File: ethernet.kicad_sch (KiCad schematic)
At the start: 27 parts, among them U5 W5500, Y1 25MHz

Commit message: Stuff.
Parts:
- C15: LCSC (none) -> C466237
- C17: LCSC (none) -> C2911388
- C4, C8: value 18p -> 22p; LCSC C555395 -> (none)
- U5: LCSC (none) -> C32843
- Y1: LCSC (none) -> C5563795
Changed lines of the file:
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@@
 			)
 		)
-		(property "Datasheet" ""
+		(property "Datasheet" "https://jlcpcb.com/partdetail/Sanyear-C0402X5R475M250NT/C2911388"
 			(at 129.54 119.38 0)
 			(effects
@@
 			)
 		)
+		(property "LCSC" "C2911388"
+			(at 129.54 119.38 0)
+			(effects
+				(font
+					(size 1.27 1.27)
+				)
+				(hide yes)
+			)
+		)
 		(pin "2"
 		)
@@
 			)
 		)
-		(property "Value" "18p"
+		(property "Value" "22p"
 			(at 210.566 100.076 0)
 			(effects
@@
 			)
 		)
-		(property "Description" "Unpolarized capacitor"
+		(property "Description" ""
 			(at 210.82 97.79 0)
 			(effects
@@
 			)
 		)
-		(property "LCSC" "C555395"
+		(property "LCSC" ""
 			(at 210.82 97.79 0)
 			(effects
@@
 			)
 		)
-		(property "Datasheet" ""
+		(property "Datasheet" "https://www.lcsc.com/product-detail/Crystal-Oscillators_HCI-1532H4-25000J18DTSTL_C5563795.html"
 			(at 205.74 90.17 0)
 			(effects
@@
 			)
 		)
-		(property "LCSC" ""
+		(property "LCSC" "C5563795"
 			(at 205.74 90.17 0)
 			(effects
@@
 			)
 		)
-		(property "Datasheet" ""
+		(property "Datasheet" "https://jlcpcb.com/partdetail/Cctc-TCC0402X7R223K250AT/C466237"
 			(at 143.51 90.17 0)
 			(effects
@@
 			)
 		)
+		(property "LCSC" "C466237"
+			(at 143.51 90.17 0)
+			(effects
+				(font
+					(size 1.27 1.27)
+				)
+				(hide yes)
+			)
+		)
 		(pin "2"
 		)
@@
 			)
 		)
+		(property "LCSC" "C32843"
+			(at 172.72 86.36 0)
+			(effects
+				(font
+					(size 1.27 1.27)
+				)
+				(hide yes)
+			)
+		)
 		(pin "38"
 		)
@@
 			)
 		)
-		(property "Value" "18p"
+		(property "Value" "22p"
 			(at 200.406 100.076 0)
 			(effects
@@
 			)
 		)
-		(property "Description" "Unpolarized capacitor"
+		(property "Description" ""
 			(at 200.66 97.79 0)
 			(effects
@@
 			)
 		)
-		(property "LCSC" "C555395"
+		(property "LCSC" ""
 			(at 200.66 97.79 0)
 			(effects

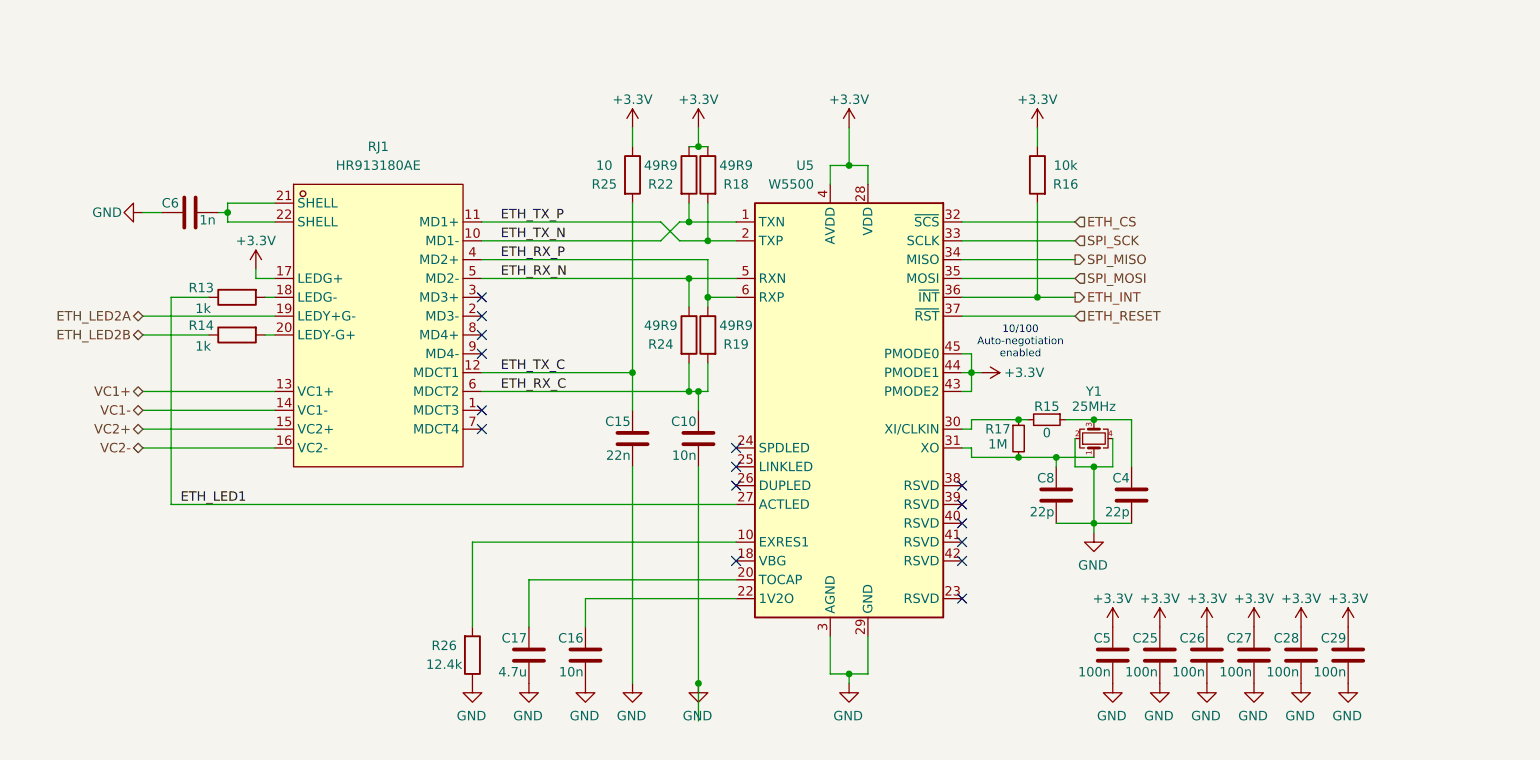
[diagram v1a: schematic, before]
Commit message: added 3D models, added LCSC numbers, added caps in RX line ethernet as per the datasheet, change crystal and capacitors to correctly match w5500 as per the datasheet, added bead to filter analoge power supply for w5500 as per the datasheet, added filter for the ina2XX for beter monitoring
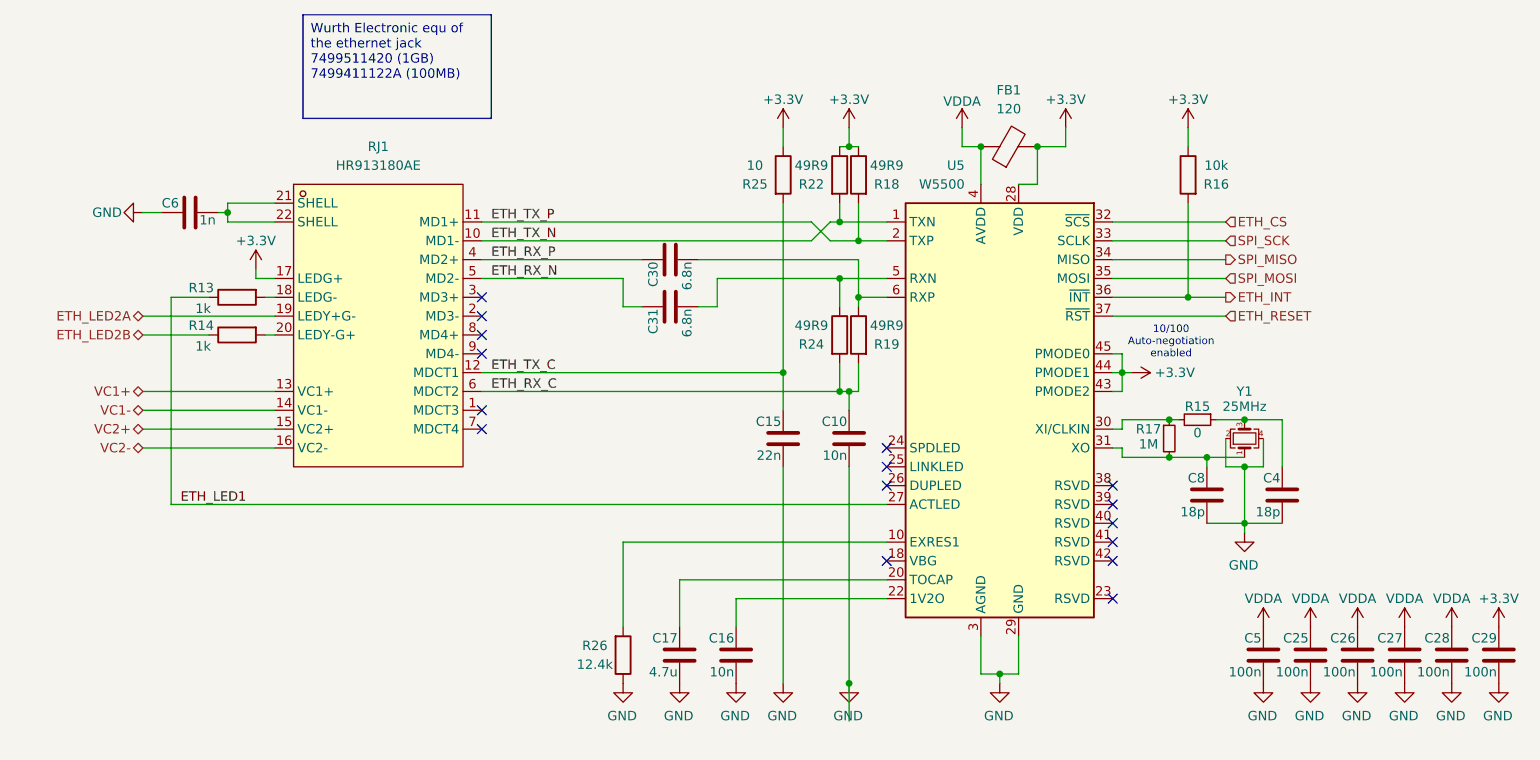
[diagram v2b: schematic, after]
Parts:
- added C30, C31: 6.8n, Capacitor_SMD:C_0402_1005Metric, symbol Device:C
- added FB1: 120, Inductor_SMD:L_0603_1608Metric, symbol Device:FerriteBead
- C4, C8: value 22p -> 18p; LCSC (none) -> C555395
- R13, R14: LCSC (none) -> C2935237
- R15: LCSC (none) -> C17168
- R17: LCSC (none) -> C26083
- R18, R19, R22, R24: LCSC (none) -> C25120
- R25: LCSC (none) -> C138066
- R26: LCSC (none) -> C284314
- Y1: LCSC C5563795 -> C7275110
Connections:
- net +3.3V: now also FB1.2; no longer C25.1, C26.1, C27.1, C28.1, C5.1, U5.11 (AVDD), U5.15 (AVDD), U5.17 (AVDD), U5.21 (AVDD), U5.4 (AVDD), U5.8 (AVDD)
- net ETH_RX_N: now also C31.1; no longer R24.1, U5.5 (RXN)
- net ETH_RX_P: now also C30.1; no longer R19.1, U5.6 (RXP)
- new net: C30.2, R19.1, U5.6 (RXP)
- new net: C31.2, R24.1, U5.5 (RXN)
- new net VDDA: C25.1, C26.1, C27.1, C28.1, C5.1, FB1.1, U5.11 (AVDD), U5.15 (AVDD), U5.17 (AVDD), U5.21 (AVDD), U5.4 (AVDD), U5.8 (AVDD)
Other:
- moved on the sheet: C10, C15, C16, C17, C25, C26, C27, C28, C29, C4, C5, C8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

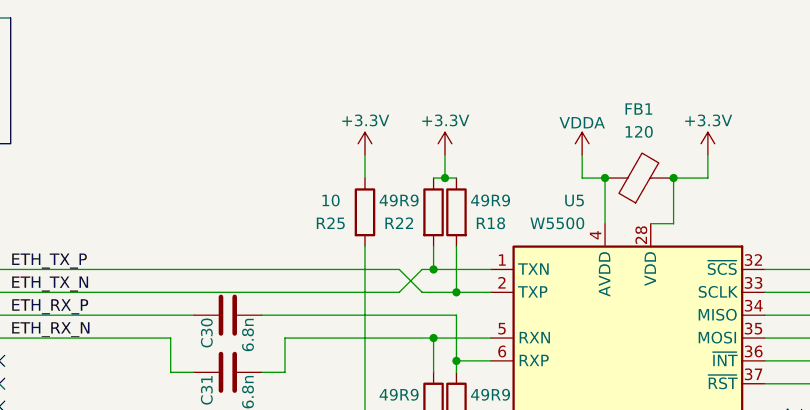
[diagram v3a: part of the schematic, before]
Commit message: Add RS485, add mounting holes, route more stuff
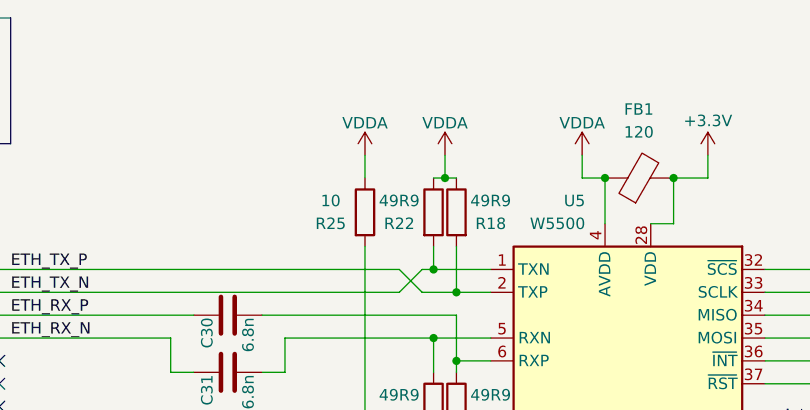
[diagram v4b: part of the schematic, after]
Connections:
- net +3.3V: no longer R18.1, R22.1, R25.1
- net VDDA: now also R18.1, R22.1, R25.1
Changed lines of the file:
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@@
+	)
+	(symbol
+		(lib_id "power:VDDA")
+		(at 172.72 48.26 0)
+		(unit 1)
+		(exclude_from_sim no)
+		(in_bom yes)
+		(on_board yes)
+		(dnp no)
+		(property "Reference" "#PWR041"
+			(at 172.72 52.07 0)
+			(effects
+				(font
+					(size 1.27 1.27)
+				)
+				(hide yes)
+			)
+		)
+		(property "Value" "VDDA"
+			(at 172.72 44.704 0)
+			(effects
+				(font
+					(size 1.27 1.27)
+				)
+			)
+		)
+		(property "Footprint" ""
+			(at 172.72 48.26 0)
+			(effects
+				(font
+					(size 1.27 1.27)
+				)
+				(hide yes)
+			)
+		)
+		(property "Datasheet" ""
+			(at 172.72 48.26 0)
+			(effects
+				(font
+					(size 1.27 1.27)
+				)
+				(hide yes)
+			)
+		)
+		(property "Description" "Power symbol creates a global label with name \"VDDA\""
+			(at 172.72 48.26 0)
+			(effects
+				(font
+					(size 1.27 1.27)
+				)
+				(hide yes)
+			)
+		)
+		(pin "1"
+		)
+		(instances
+			(project "whylight"
+				(path "/12ab2aee-f6e3-4178-94ff-8d6a84db0790/65e3049f-1cb2-47b8-b429-83c99da9f6f6"
+					(reference "#PWR041")
+					(unit 1)
+				)
+			)
+		)
 	)
 	(symbol
@@
 	)
 	(symbol
+		(lib_id "power:VDDA")
+		(at 163.83 48.26 0)
+		(unit 1)
+		(exclude_from_sim no)
+		(in_bom yes)
+		(on_board yes)
+		(dnp no)
+		(property "Reference" "#PWR039"
+			(at 163.83 52.07 0)
+			(effects
+				(font
+					(size 1.27 1.27)
+				)
+				(hide yes)
+			)
+		)
+		(property "Value" "VDDA"
+			(at 163.83 44.704 0)
+			(effects
+				(font
+					(size 1.27 1.27)
+				)
+			)
+		)
+		(property "Footprint" ""
+			(at 163.83 48.26 0)
+			(effects
+				(font
+					(size 1.27 1.27)
+				)
+				(hide yes)
+			)
+		)
+		(property "Datasheet" ""
+			(at 163.83 48.26 0)
+			(effects
+				(font
+					(size 1.27 1.27)
+				)
+				(hide yes)
+			)
+		)
+		(property "Description" "Power symbol creates a global label with name \"VDDA\""
+			(at 163.83 48.26 0)
+			(effects
+				(font
+					(size 1.27 1.27)
+				)
+				(hide yes)
+			)
+		)
+		(pin "1"
+		)
+		(instances
+			(project "whylight"
+				(path "/12ab2aee-f6e3-4178-94ff-8d6a84db0790/65e3049f-1cb2-47b8-b429-83c99da9f6f6"
+					(reference "#PWR039")
+					(unit 1)
+				)
+			)
+		)
+	)
+	(symbol
 		(lib_id "Device:C")
 		(at 163.83 90.17 0)
@@
 	)
 	(symbol
-		(lib_id "power:+3.3V")
-		(at 163.83 48.26 0)
-		(mirror y)
-		(unit 1)
-		(exclude_from_sim no)
-		(in_bom yes)
-		(on_board yes)
-		(dnp no)
-		(property "Reference" "#PWR041"
-			(at 163.83 52.07 0)
-			(effects
-				(font
-					(size 1.27 1.27)
-				)
-				(hide yes)
-			)
-		)
-		(property "Value" "+3.3V"
-			(at 163.83 44.45 0)
-			(effects
-				(font
-					(size 1.27 1.27)
-				)
-			)
-		)
-		(property "Footprint" ""
-			(at 163.83 48.26 0)
-			(effects
-				(font
-					(size 1.27 1.27)
-				)
-				(hide yes)
-			)
-		)
-		(property "Datasheet" ""
-			(at 163.83 48.26 0)
-			(effects
-				(font
-					(size 1.27 1.27)
-				)
-				(hide yes)
-			)
-		)
-		(property "Description" "Power symbol creates a global label with name \"+3.3V\""
-			(at 163.83 48.26 0)
-			(effects
-				(font
-					(size 1.27 1.27)
-				)
-				(hide yes)
-			)
-		)
-		(pin "1"
-		)
-		(instances
-			(project "whylight"
-				(path "/12ab2aee-f6e3-4178-94ff-8d6a84db0790/65e3049f-1cb2-47b8-b429-83c99da9f6f6"
-					(reference "#PWR041")
-					(unit 1)
-				)
-			)
-		)
-	)
-	(symbol
 		(lib_id "symbols:R")
 		(at 163.83 54.61 0)
@@
 					(unit 1)
 				)
-			)
-		)
-	)
-	(symbol
-		(lib_id "power:+3.3V")
-		(at 172.72 48.26 0)
-		(mirror y)
-		(unit 1)
-		(exclude_from_sim no)
-		(in_bom yes)
-		(on_board yes)
-		(dnp no)
-		(property "Reference" "#PWR039"
-			(at 172.72 52.07 0)
-			(effects
-				(font
-					(size 1.27 1.27)
-				)
-				(hide yes)
-			)
-		)
-		(property "Value" "+3.3V"
-			(at 172.72 44.45 0)
-			(effects
-				(font
-					(size 1.27 1.27)
-				)
-			)
-		)
-		(property "Footprint" ""
-			(at 172.72 48.26 0)
-			(effects
-				(font
-					(size 1.27 1.27)
-				)
-				(hide yes)
-			)
-		)
-		(property "Datasheet" ""
-			(at 172.72 48.26 0)
-			(effects
-				(font
-					(size 1.27 1.27)
-				)
-				(hide yes)
-			)
-		)
-		(property "Description" "Power symbol creates a global label with name \"+3.3V\""
-			(at 172.72 48.26 0)
-			(effects
-				(font
-					(size 1.27 1.27)
-				)
-				(hide yes)
-			)
-		)
-		(pin "1"
-		)
-		(instances
-			(project "whylight"
-				(path "/12ab2aee-f6e3-4178-94ff-8d6a84db0790/65e3049f-1cb2-47b8-b429-83c99da9f6f6"
-					(reference "#PWR039")
-					(unit 1)
-				)

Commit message: Release r0.1
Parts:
- removed RJ1: HR913180AE, library:RJ45-TH_HR913180AE, symbol RJ45-TH_HR913180AE:HR913180AE
- added J6: 0826-1X1T-GJ-F, library:BEL_0826-1X1T-GJ-F, symbol 0826-1X1T-GJ-F:0826-1X1T-GJ-F
- C17: LCSC C2911388 -> C307423
- R13, R14: LCSC C2935237 -> C11702
- Y1: LCSC C7275110 -> C7424735
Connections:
- net +3.3V: now also J6.18
- net ETH_LED2A: now also J6.19
- net ETH_RX_C: now also J6.6 (TRCT2)
- net ETH_RX_N: now also J6.5 (TRD2-)
- net ETH_RX_P: now also J6.4 (TRD2+)
- net ETH_TX_C: now also J6.12 (TRCT1)
- net ETH_TX_N: now also J6.10 (TRD1-)
- net ETH_TX_P: now also J6.11 (TRD1+)
- net VC1+: now also J6.13 (VC12)
- net VC1-: now also J6.14 (VC36)
- net VC2+: now also J6.15 (VC45)
- net VC2-: now also J6.16 (VC78)
- net at R14.2: now also J6.20
- net at C6.1: now also J6.S1 (SHIELD), J6.S2 (SHIELD)
- net at R13.2: now also J6.17
- no-connect marks 16 -> 10
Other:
- moved on the sheet: C10, C15, C16, C17, C25, C26, C27, C28, C29, C30, C31, C4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
